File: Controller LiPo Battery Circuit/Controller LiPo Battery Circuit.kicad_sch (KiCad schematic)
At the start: 37 parts, among them CN1 USBA_FEMALE, J1 Jack-DC, Q1 MMUN2133LT1G, U1 TPS61090RSAR, U2 MCP73831T-2ACI/OT, X1 TERMBLOCK_1X2, X2 microUSB

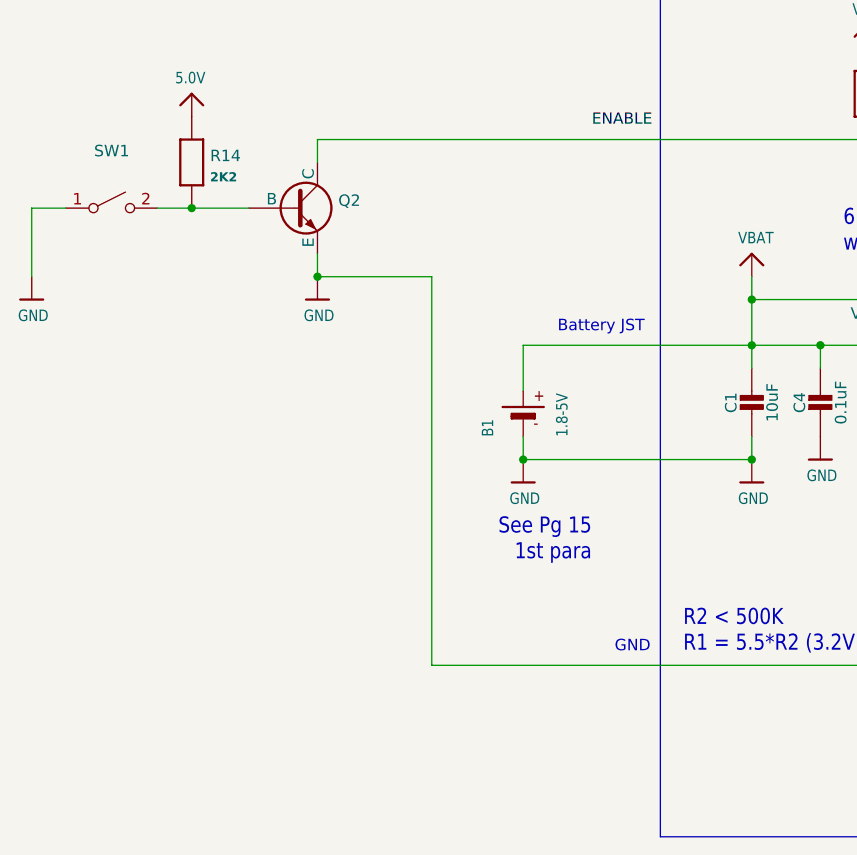
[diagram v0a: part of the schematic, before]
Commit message: Added in LBO transistor
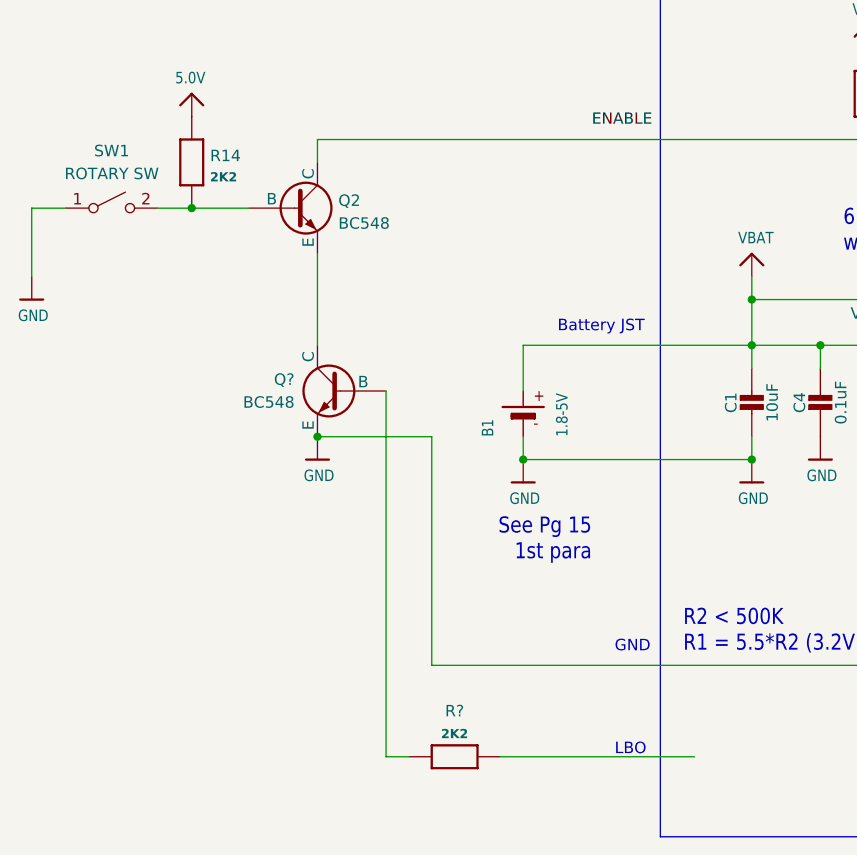
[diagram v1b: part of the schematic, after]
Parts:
- added Q?: BC548, Package_TO_SOT_THT:TO-92_Inline, symbol Transistor_BJT:BC548
- added R?: 2K2, Controller LiPo Battery Circuit:0603-MINI, symbol Controller LiPo Battery Circuit-eagle-import:RESISTOR0603MINI
- Q2: value (none) -> BC548; footprint (none) -> Package_TO_SOT_THT:TO-92_Inline
- SW1: value (none) -> ROTARY SW
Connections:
- net GND: now also Q?.3 (E); no longer Q2.3 (E)
- new net: Q2.3 (E), Q?.1 (C)
- new net: Q?.2 (B), R?.2
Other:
- note added: "LBO"
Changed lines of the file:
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@@
   (junction (at 214.63 111.76) (diameter 0) (color 0 0 0 0)
   )
+  (junction (at 80.01 142.24) (diameter 0) (color 0 0 0 0)
+  )
   (junction (at 135.89 132.08) (diameter 0) (color 0 0 0 0)
   )
@@
   (junction (at 191.77 147.32) (diameter 0) (color 0 0 0 0)
   )
-  (junction (at 80.01 124.46) (diameter 0) (color 0 0 0 0)
-  )
   (junction (at 214.63 127) (diameter 0) (color 0 0 0 0)
   )
@@
     (stroke (width 0) (type default) (color 0 0 0 0))
   )
+  (wire (pts (xy 92.71 167.64) (xy 92.71 142.24))
+    (stroke (width 0) (type default) (color 0 0 0 0))
+  )
   (wire (pts (xy 102.87 132.08) (xy 102.87 137.16))
     (stroke (width 0) (type default) (color 0 0 0 0))
@@
     (stroke (width 0) (type default) (color 0 0 0 0))
   )
-  (wire (pts (xy 80.01 121.92) (xy 80.01 124.46))
+  (wire (pts (xy 80.01 121.92) (xy 80.01 132.08))
+    (stroke (width 0) (type default) (color 0 0 0 0))
+  )
+  (wire (pts (xy 92.71 142.24) (xy 80.01 142.24))
     (stroke (width 0) (type default) (color 0 0 0 0))
   )
@@
     (stroke (width 0) (type default) (color 0 0 0 0))
   )
+  (wire (pts (xy 87.63 137.16) (xy 87.63 177.8))
+    (stroke (width 0) (type default) (color 0 0 0 0))
+  )
   (wire (pts (xy 293.37 78.74) (xy 293.37 71.12))
     (stroke (width 0) (type default) (color 0 0 0 0))
@@
     (stroke (width 0) (type default) (color 0 0 0 0))
   )
-  (wire (pts (xy 80.01 124.46) (xy 92.71 124.46))
-    (stroke (width 0) (type default) (color 0 0 0 0))
-  )
   (wire (pts (xy 370.84 143.51) (xy 370.84 144.78))
     (stroke (width 0) (type default) (color 0 0 0 0))
@@
     (stroke (width 0) (type default) (color 0 0 0 0))
   )
+  (wire (pts (xy 100.33 177.8) (xy 121.92 177.8))
+    (stroke (width 0) (type default) (color 0 0 0 0))
+  )
   (wire (pts (xy 245.11 76.2) (xy 250.19 76.2))
     (stroke (width 0) (type default) (color 0 0 0 0))
@@
     (stroke (width 0) (type default) (color 0 0 0 0))
   )
+  (wire (pts (xy 87.63 177.8) (xy 90.17 177.8))
+    (stroke (width 0) (type default) (color 0 0 0 0))
+  )
   (wire (pts (xy 219.71 55.88) (xy 250.19 55.88))
     (stroke (width 0) (type default) (color 0 0 0 0))
@@
   )
   (wire (pts (xy 161.29 137.16) (xy 148.59 137.16))
-    (stroke (width 0) (type default) (color 0 0 0 0))
-  )
-  (wire (pts (xy 92.71 124.46) (xy 92.71 167.64))
     (stroke (width 0) (type default) (color 0 0 0 0))
   )
@@
   )
   (text "To Controller\n" (at 377.19 143.51 0)
+    (effects (font (size 1.27 1.27)) (justify left bottom))
+  )
+  (text "LBO\n" (at 113.03 177.8 0)
     (effects (font (size 1.27 1.27)) (justify left bottom))
   )
@@
     (pin "P$2")
   )
-  (symbol (lib_id "Controller LiPo Battery Circuit-eagle-import:GND") (at 80.01 127 0) (unit 1)
-    (in_bom yes) (on_board yes)
-    (property "Reference" "#U$013" (id 0) (at 80.01 127 0)
-      (effects (font (size 1.27 1.27)) hide)
-    )
-    (property "Value" "GND" (id 1) (at 78.486 129.54 0)
-      (effects (font (size 1.27 1.0795)) (justify left bottom))
-    )
-    (property "Footprint" "Controller LiPo Battery Circuit:" (id 2) (at 80.01 127 0)
-      (effects (font (size 1.27 1.27)) hide)
-    )
-    (property "Datasheet" "" (id 3) (at 80.01 127 0)
-      (effects (font (size 1.27 1.27)) hide)
-    )
-    (pin "1")
-  )
   (symbol (lib_id "Switch:SW_SPST") (at 57.15 116.84 0) (unit 1)
     (in_bom yes) (on_board yes) (fields_autoplaced)
     (property "Reference" "SW1" (id 0) (at 57.15 110.49 0))
-    (property "Value" "" (id 1) (at 57.15 113.03 0))
+    (property "Value" "ROTARY SW" (id 1) (at 57.15 113.03 0))
     (property "Footprint" "" (id 2) (at 57.15 116.84 0)
       (effects (font (size 1.27 1.27)) hide)
@@
     (pin "E")
   )
+  (symbol (lib_id "Transistor_BJT:BC548") (at 82.55 137.16 0) (mirror y) (unit 1)
+    (in_bom yes) (on_board yes) (fields_autoplaced)
+    (property "Reference" "Q?" (id 0) (at 77.47 135.8899 0)
+      (effects (font (size 1.27 1.27)) (justify left))
+    )
+    (property "Value" "BC548" (id 1) (at 77.47 138.4299 0)
+      (effects (font (size 1.27 1.27)) (justify left))
+    )
+    (property "Footprint" "Package_TO_SOT_THT:TO-92_Inline" (id 2) (at 77.47 139.065 0)
+      (effects (font (size 1.27 1.27) italic) (justify left) hide)
+    )
+    (property "Datasheet" "https://www.onsemi.com/pub/Collateral/BC550-D.pdf" (id 3) (at 82.55 137.16 0)
+      (effects (font (size 1.27 1.27)) (justify left) hide)
+    )
+    (pin "1")
+    (pin "2")
+    (pin "3")
+  )
   (symbol (lib_id "Controller LiPo Battery Circuit-eagle-import:VBAT") (at 140.97 96.52 0) (unit 1)
     (in_bom yes) (on_board yes)
@@
     (pin "1")
     (pin "2")
+  )
+  (symbol (lib_id "Controller LiPo Battery Circuit-eagle-import:GND") (at 80.01 144.78 0) (unit 1)
+    (in_bom yes) (on_board yes)
+    (property "Reference" "#U$?" (id 0) (at 80.01 144.78 0)
+      (effects (font (size 1.27 1.27)) hide)
+    )
+    (property "Value" "GND" (id 1) (at 78.486 147.32 0)
+      (effects (font (size 1.27 1.0795)) (justify left bottom))
+    )
+    (property "Footprint" "Controller LiPo Battery Circuit:" (id 2) (at 80.01 144.78 0)
+      (effects (font (size 1.27 1.27)) hide)
+    )
+    (property "Datasheet" "" (id 3) (at 80.01 144.78 0)
+      (effects (font (size 1.27 1.27)) hide)
+    )
+    (pin "1")
   )
   (symbol (lib_id "Controller LiPo Battery Circuit-eagle-import:GND") (at 260.35 83.82 0) (unit 1)
@@
       (effects (font (size 1.27 1.27)) (justify left))
     )
-    (property "Value" "" (id 1) (at 82.3214 118.5422 0)
+    (property "Value" "BC548" (id 1) (at 82.3214 118.5422 0)
       (effects (font (size 1.27 1.27)) (justify left))
     )
-    (property "Footprint" "" (id 2) (at 82.55 118.745 0)
+    (property "Footprint" "Package_TO_SOT_THT:TO-92_Inline" (id 2) (at 82.55 118.745 0)
       (effects (font (size 1.27 1.27) italic) (justify left) hide)
     )
@@
     (pin "1")
   )
+  (symbol (lib_id "Controller LiPo Battery Circuit-eagle-import:RESISTOR0603MINI") (at 95.25 177.8 180) (unit 1)
+    (in_bom yes) (on_board yes) (fields_autoplaced)
+    (property "Reference" "R?" (id 0) (at 95.25 172.72 0))
+    (property "Value" "2K2" (id 1) (at 95.25 175.26 0)
+      (effects (font (size 1.016 1.016) bold))
+    )
+    (property "Footprint" "Controller LiPo Battery Circuit:0603-MINI" (id 2) (at 95.25 177.8 0)
+      (effects (font (size 1.27 1.27)) hide)
+    )
+    (property "Datasheet" "" (id 3) (at 95.25 177.8 0)
+      (effects (font (size 1.27 1.27)) hide)
+    )
+    (pin "1")
+    (pin "2")
+  )
   (symbol (lib_id "Controller LiPo Battery Circuit-eagle-import:RESISTOR0805_NOOUTLINE") (at 191.77 142.24 90) (unit 1)
     (in_bom yes) (on_board yes)
@@
       (reference "#U$012") (unit 1) (value "5.0V") (footprint "Controller LiPo Battery Circuit:")
     )
-    (path "/0f924090-ddb0-4e05-904c-8a63a32e091d"
-      (reference "#U$013") (unit 1) (value "GND") (footprint "Controller LiPo Battery Circuit:")
-    )
     (path "/ade89231-6ba7-419e-8ac3-7617b21c9ae1"
       (reference "#U$014") (unit 1) (value "GND") (footprint "Controller LiPo Battery Circuit:")
@@
       (reference "#U$034") (unit 1) (value "VBAT") (footprint "Controller LiPo Battery Circuit:")
     )
+    (path "/45b61e08-fb8b-424f-9af8-ec5f130db00b"
+      (reference "#U$?") (unit 1) (value "GND") (footprint "Controller LiPo Battery Circuit:")
+    )
     (path "/f9f226e5-0a42-4655-bcec-69756c4cbf10"
       (reference "B1") (unit 1) (value "1.8-5V") (footprint "Controller LiPo Battery Circuit:JSTPH2")
@@
       (reference "Q2") (unit 1) (value "BC548") (footprint "Package_TO_SOT_THT:TO-92_Inline")
     )
+    (path "/2c106d57-d126-491f-b8e5-3d7b48ca676e"
+      (reference "Q?") (unit 1) (value "BC548") (footprint "Package_TO_SOT_THT:TO-92_Inline")
+    )
     (path "/adda07ce-daac-4e4e-9d52-415971c89ae0"
       (reference "R1") (unit 1) (value "1.87Mohm") (footprint "Controller LiPo Battery Circuit:0805-NO")
@@
       (reference "R20") (unit 1) (value "1K") (footprint "Controller LiPo Battery Circuit:0805-NO")
     )
+    (path "/d76d002d-79a6-493d-beee-cfd6c20e9189"
+      (reference "R?") (unit 1) (value "2K2") (footprint "Controller LiPo Battery Circuit:0603-MINI")
+    )
     (path "/1815e0a6-d6ea-443e-92b7-f4945f548a6a"
